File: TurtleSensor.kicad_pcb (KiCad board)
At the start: 2 copper layers, 30 x 30 mm, 13 parts, among them IC1 ATMEGA328P-A, J1 ISPConnector, J2 FTDIConnector, U1 SI7021, U2 W25Q32FVSSIG

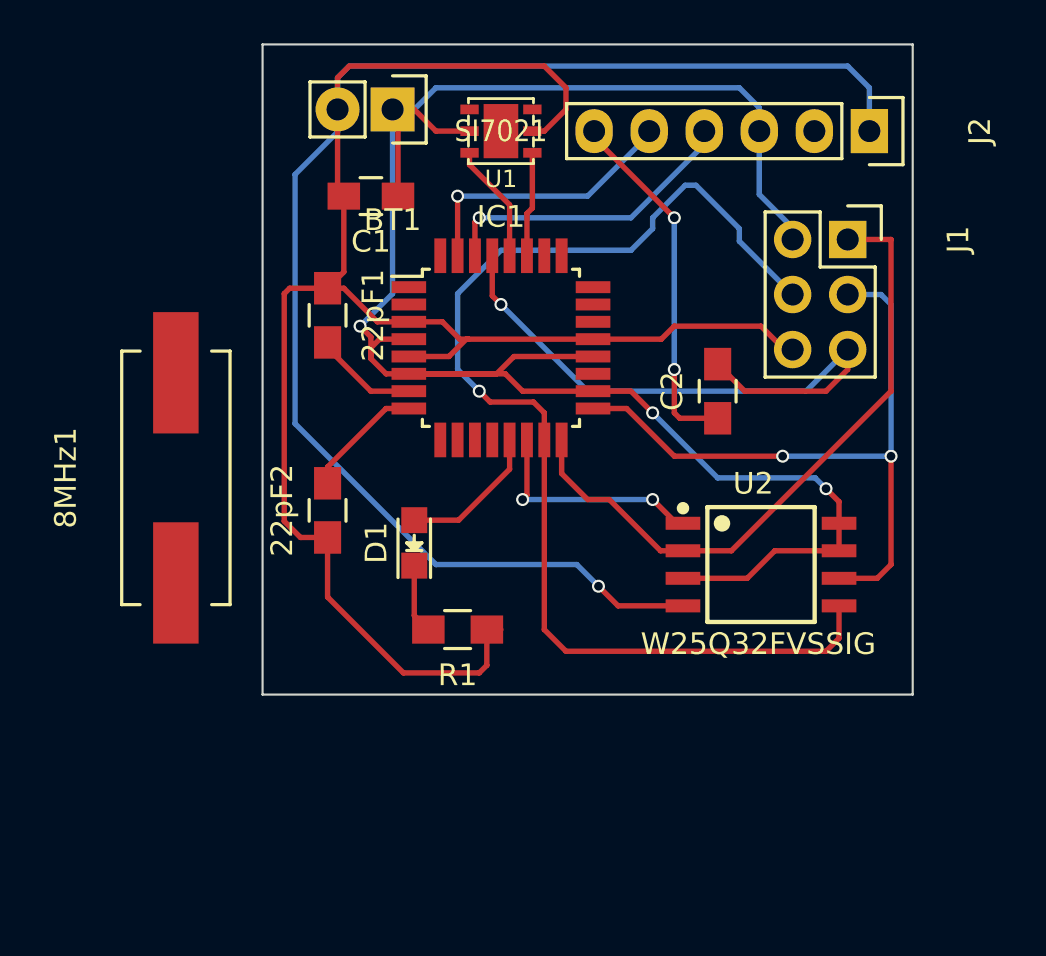
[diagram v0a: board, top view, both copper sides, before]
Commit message: pads underneath flash short
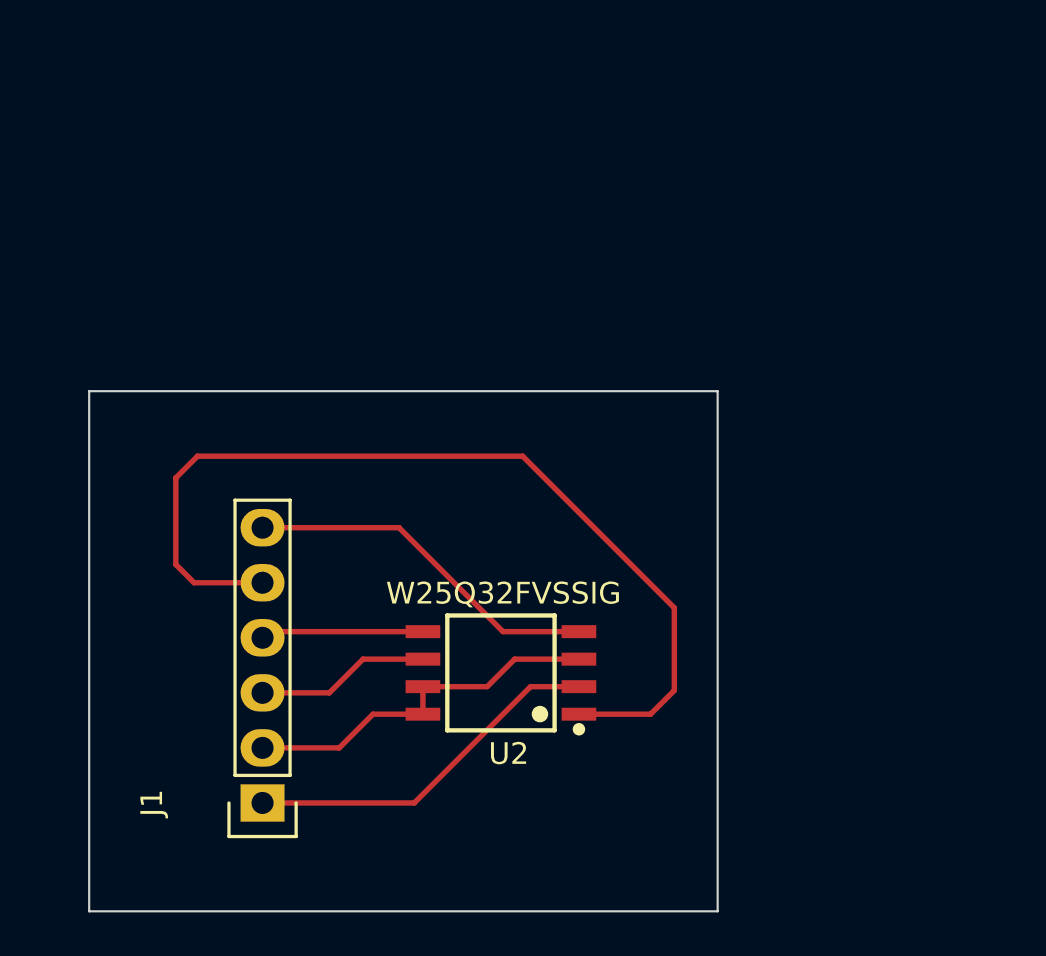
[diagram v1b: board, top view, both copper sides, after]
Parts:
- removed 22pF1, 22pF2: C, Capacitors_SMD:C_0805_HandSoldering
- removed 8MHz1: Crystal, Crystals:Crystal_HC49-SD_SMD
- removed BT1: Battery, Socket_Strips:Socket_Strip_Straight_1x02
- removed C1: 10µF, Capacitors_SMD:C_0805_HandSoldering
- removed C2: 0.1uF, Capacitors_SMD:C_0805_HandSoldering
- removed D1: LED, LEDs:LED_0805
- removed IC1: ATMEGA328P-A, Housings_QFP:TQFP-32_7x7mm_Pitch0.8mm
- removed J2: FTDIConnector, Pin_Headers:Pin_Header_Straight_1x06
- removed R1: 470, Resistors_SMD:R_0805_HandSoldering
- removed U1: SI7021, SI7021:DFN-6%2f3MM
- J1: footprint Socket_Strips:Socket_Strip_Straight_2x03 -> Socket_Strips:Socket_Strip_Straight_1x06
- moved J1 37.5 mm to (130.0, 113.0), turned to 90 degrees
- moved U2 13.0 mm to (141.0, 107.0), turned to 180 degrees
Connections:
- J1 pad 5: /~RST -> /~CS
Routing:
- net GND: track 144.7 -> 16.6 mm, vias 1 -> 0
- net +BATT: track 90.4 -> 17.0 mm, vias 3 -> 0
- net /MOSI: track 54.3 -> 7.52 mm, vias 1 -> 0
- net /~CS: track 10.7 -> 43.3 mm, vias 2 -> 0
- net /~RST: track 28.7 -> 0.00 mm, vias 1 -> 0
- net /SCK: track 31.5 -> 8.04 mm, vias 2 -> 0
- net Net-(C2-Pad1): track 17.3 -> 0.00 mm, vias 2 -> 0
- net /RX: track 14.2 -> 0.00 mm, vias 1 -> 0
- net /TX: track 13.7 -> 0.00 mm, vias 1 -> 0
- net /MISO: track 30.3 -> 16.8 mm
- net Net-(D1-Pad2): track 6.72 -> 0.00 mm
- net /SCL: track 5.73 -> 0.00 mm
- net Net-(22pF2-Pad2): track 5.62 -> 0.00 mm
- net /SDA: track 4.85 -> 0.00 mm
- net Net-(22pF1-Pad2): track 4.83 -> 0.00 mm
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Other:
- board size 30 x 30 mm -> 29 x 24 mm
- net class Default: clearance 0.2 -> 0.25
- rule trace_clearance: 0.2 -> 0.25
- rule trace_min: 0.2 -> 0.25
